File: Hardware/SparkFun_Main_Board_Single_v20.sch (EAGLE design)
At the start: 84 parts, among them J1 MICROMOD-2222-C, J10 MICRO-SD-PUSH-PUSH-EXT-PIN, J2 Vertical Qwiic Connector, J4 QWIIC_RIGHT_ANGLE, J5 CORTEX_JTAG_DEBUG_MINIMUM_PTH, J6 MICROMOD_FUNCTION_MAIN, Q1 3.1A/30V/105mΩ, Q2 20V/4.2A/52mΩ/1.4W, U1 STG3856QTR, U2 MCP73831, U3 ESD Diode, U4 AP7347DQ-33W5-7K-3.3V, U5 AP7361C-33

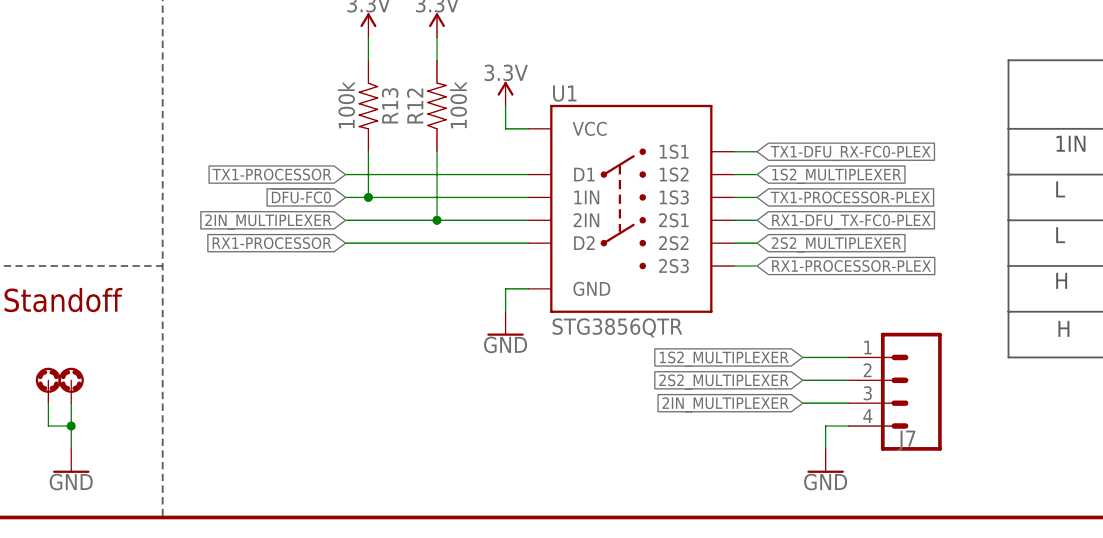
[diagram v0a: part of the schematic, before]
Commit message: Updates silk on multiplexing PTH
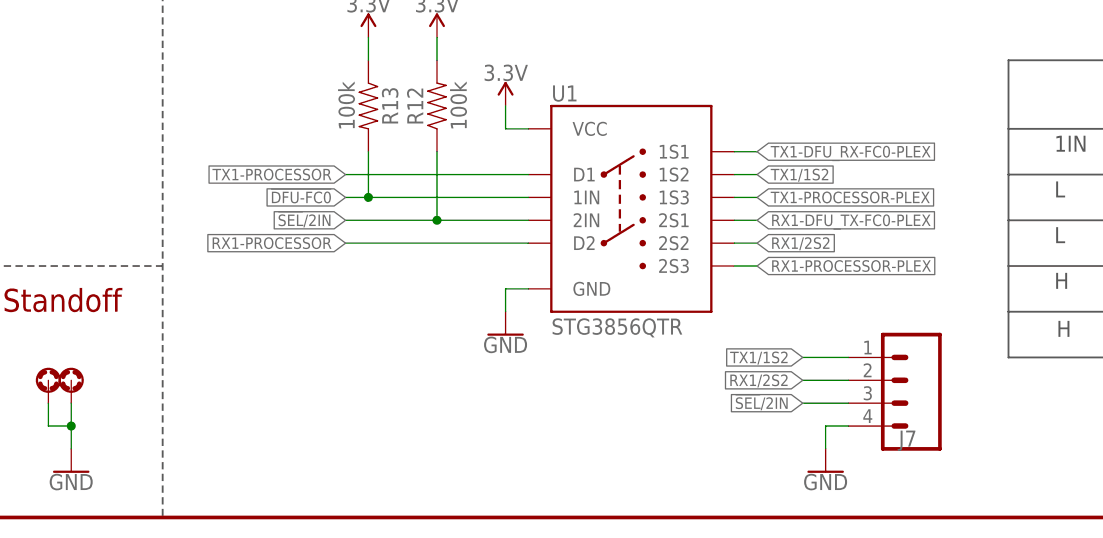
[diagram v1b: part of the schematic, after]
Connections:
- net 1S2_MULTIPLEXER renamed TX1/1S2
- net 2IN_MULTIPLEXER renamed !SEL!/2IN
- net 2S2_MULTIPLEXER renamed RX1/2S2
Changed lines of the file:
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@@
 </segment>
 </net>
-<net name="2S2_MULTIPLEXER" class="0">
+<net name="RX1/2S2" class="0">
 <segment>
 <pinref part="U1" gate="G$1" pin="2S2"/>
@@
 </segment>
 </net>
-<net name="1S2_MULTIPLEXER" class="0">
+<net name="TX1/1S2" class="0">
 <segment>
 <pinref part="U1" gate="G$1" pin="1S2"/>
@@
 </segment>
 </net>
-<net name="2IN_MULTIPLEXER" class="0">
+<net name="!SEL!/2IN" class="0">
 <segment>
 <pinref part="J7" gate="J1" pin="3"/>
